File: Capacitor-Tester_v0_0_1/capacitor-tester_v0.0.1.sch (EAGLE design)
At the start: 34 parts, among them IC1 AD8531ARZ, IC2 MC34063EBD-TR, IC3 DAC6571IDBVT, IC5 AD8397ARDZ, J1 USB4125-GF-A-0190_REVA2, J2 DS1044-140G, J4 250-103, U1 AD5933, Y1 LFSPXO018034

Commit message: v0.0.1 - CMD renumber + tnames + bnames
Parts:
- removed IC5: AD8397ARDZ, AD8397ARDZ:AD8397ARDZ
- removed J4: 250-103, custom_library:250-103
- removed R15, R16: 10k-1%, custom_library:RESISTOR_SMD0603
- added IC4: MC34063EBD-TR, MC34063EBD-TR:MC34063EBD-TR
- added J3: USB4125-GF-A-0190_REVA2, USB-C-6Pin:USB4125-GF-A-0190_REVA2
- added R7, R8: DNP-4k7-1%, custom_library:RESISTOR_SMD0603
- C2: value 10u -> 100n
- C3: value 100n -> 10u
- C4: value 270u / 16V -> 10u; device EEEFKC271XSP:EEEFKC271XSP -> custom_library:CAPACITOR_SMD_CERAMIC0603
- C5: value 270u / 16V -> 100n; device EEEFKC271XSP:EEEFKC271XSP -> custom_library:CAPACITOR_SMD_CERAMIC0603
- C6: value 560p -> 270u / 16V; device custom_library:CAPACITOR_SMD_CERAMIC0603 -> EEEFKC271XSP:EEEFKC271XSP
- C7: value 100n -> 560p
- C8: value 10u -> 270u / 16V; device custom_library:CAPACITOR_SMD_CERAMIC0603 -> EEEFKC271XSP:EEEFKC271XSP
- D1: value SS14 -> PMEG6020ER,115; device SS14:SS14 -> PMEG6020ER_115:PMEG6020ER,115
- D2: value PMEG6020ER,115 -> SS14; device PMEG6020ER_115:PMEG6020ER,115 -> SS14:SS14
- IC1: value AD8531ARZ -> DAC6571IDBVT; device AD8531ARZ:AD8531ARZ -> DAC6571IDBVT:DAC6571IDBVT
- IC2: value MC34063EBD-TR -> AD8397ARDZ; device MC34063EBD-TR:MC34063EBD-TR -> AD8397ARDZ:AD8397ARDZ
- IC3: value DAC6571IDBVT -> AD8531ARZ; device DAC6571IDBVT:DAC6571IDBVT -> AD8531ARZ:AD8531ARZ
- J1: value USB4125-GF-A-0190_REVA2 -> DS1044-140G; device USB-C-6Pin:USB4125-GF-A-0190_REVA2 -> DS1044-140G:DS1044-140G
- J2: value DS1044-140G -> 250-103; device DS1044-140G:DS1044-140G -> custom_library:250-103
- R1, R3: value DNP-4k7-1% -> 10k-1%
- R10: value 1k-1% -> R133-1%
- R11: value R133-1% -> 8k66-1%
- R12: value 180R-1% -> 1k-1%
- R2: value 10k-1% -> DNP-10k-1%
- R4: value DNP-10k-1% -> 1k-1%
- R6: value 1k-1% -> 10k-1%
- R9: value 8k66-1% -> 180R-1%
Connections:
- net +12V: now also C1.1, C6.+, D2.K, IC2.+VS, R11.1; no longer C3.1, C4.+, D1.K, IC5.+VS, R9.1
- net +5V: now also C3.1, C4.1, C5.1, C8.+, D1.K, IC1.VDD, IC3.V+, IC4.VCC, J3.VBUS, R10.1, R7.2, R8.2; no longer C1.1, C5.+, C7.1, C8.1, D2.K, IC1.V+, IC2.VCC, IC3.VDD, J1.VBUS, R1.2, R11.1, R3.2
- net DAC_OUT: now also IC1.VOUT, IC2.+IN2; no longer IC3.VOUT, IC5.+IN2
- net FUNC_GEN: now also J2.3, SJ1.1; no longer J4.3, SJ2.1
- net GND: now also C4.2, C5.2, C6.-, C8.-, IC1.A0, IC1.GND, IC2.-VS, IC2.EP, IC3.+IN_A, IC3.V-, IC4.GND, IC4.SWE, J3.GND, J3.SHIELD, R1.2, R12.2; no longer C4.-, C5.-, C6.2, C8.2, IC1.+IN_A, IC1.V-, IC2.GND, IC2.SWE, IC3.A0, IC3.GND, IC5.-VS, IC5.EP, J1.GND, J1.SHIELD, R10.2, R15.2
- net MCLK: now also SJ2.1; no longer SJ1.1
- net N$1: now also IC3.OUT_A, R2.2, R3.1; no longer IC1.OUT_A, R2.1, R4.2
- net N$10: now also C7.1, IC4.TC; no longer C6.1, IC2.TC
- net N$11: now also IC4.IPK, R10.2, R9.2; no longer IC2.IPK, R11.2, R12.2
- net N$13: now also IC2.-IN2, R1.1, R6.2; no longer IC5.-IN2, R15.1, R16.2
- net N$4: now also IC2.-IN1, R4.1; no longer IC5.-IN1, R6.1
- net N$5: now also D2.A, IC4.SWC; no longer D1.A, IC2.SWC
- net N$7: now also IC4.CII, R11.2, R12.1; no longer IC2.CII, R10.1, R9.2
- net N$8: now also IC4.DRC, R9.1; no longer IC2.DRC, R12.1
- net SCL: now also IC1.SCL, J2.2, R8.1; no longer IC3.SCL, J4.2, R1.1
- net SDA: now also IC1.SDA, J2.1, R7.1; no longer IC3.SDA, J4.1, R3.1
- net UZA_OUT: now also IC2.OUT1, J1.1, J1.2, J1.3, J1.4, J1.5, J1.6, J1.7, R4.2; no longer IC5.OUT1, J2.1, J2.2, J2.3, J2.4, J2.5, J2.6, J2.7, R6.2
- net UZB_OUT: now also IC2.+IN1, IC2.OUT2, R6.1; no longer IC5.+IN1, IC5.OUT2, R16.1
- net VIN: now also R2.1; no longer R4.1
- net Z_OUT: now also D1.A, IC3.-IN_A, J1.10, J1.11, J1.12, J1.13, J1.14, J1.8, J1.9, R3.2; no longer D2.A, IC1.-IN_A, J2.10, J2.11, J2.12, J2.13, J2.14, J2.8, J2.9, R2.2
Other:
- moved on the sheet: C1, C2, C3, C7, D1, D2, R1, R10, R11, R12, R2, R3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

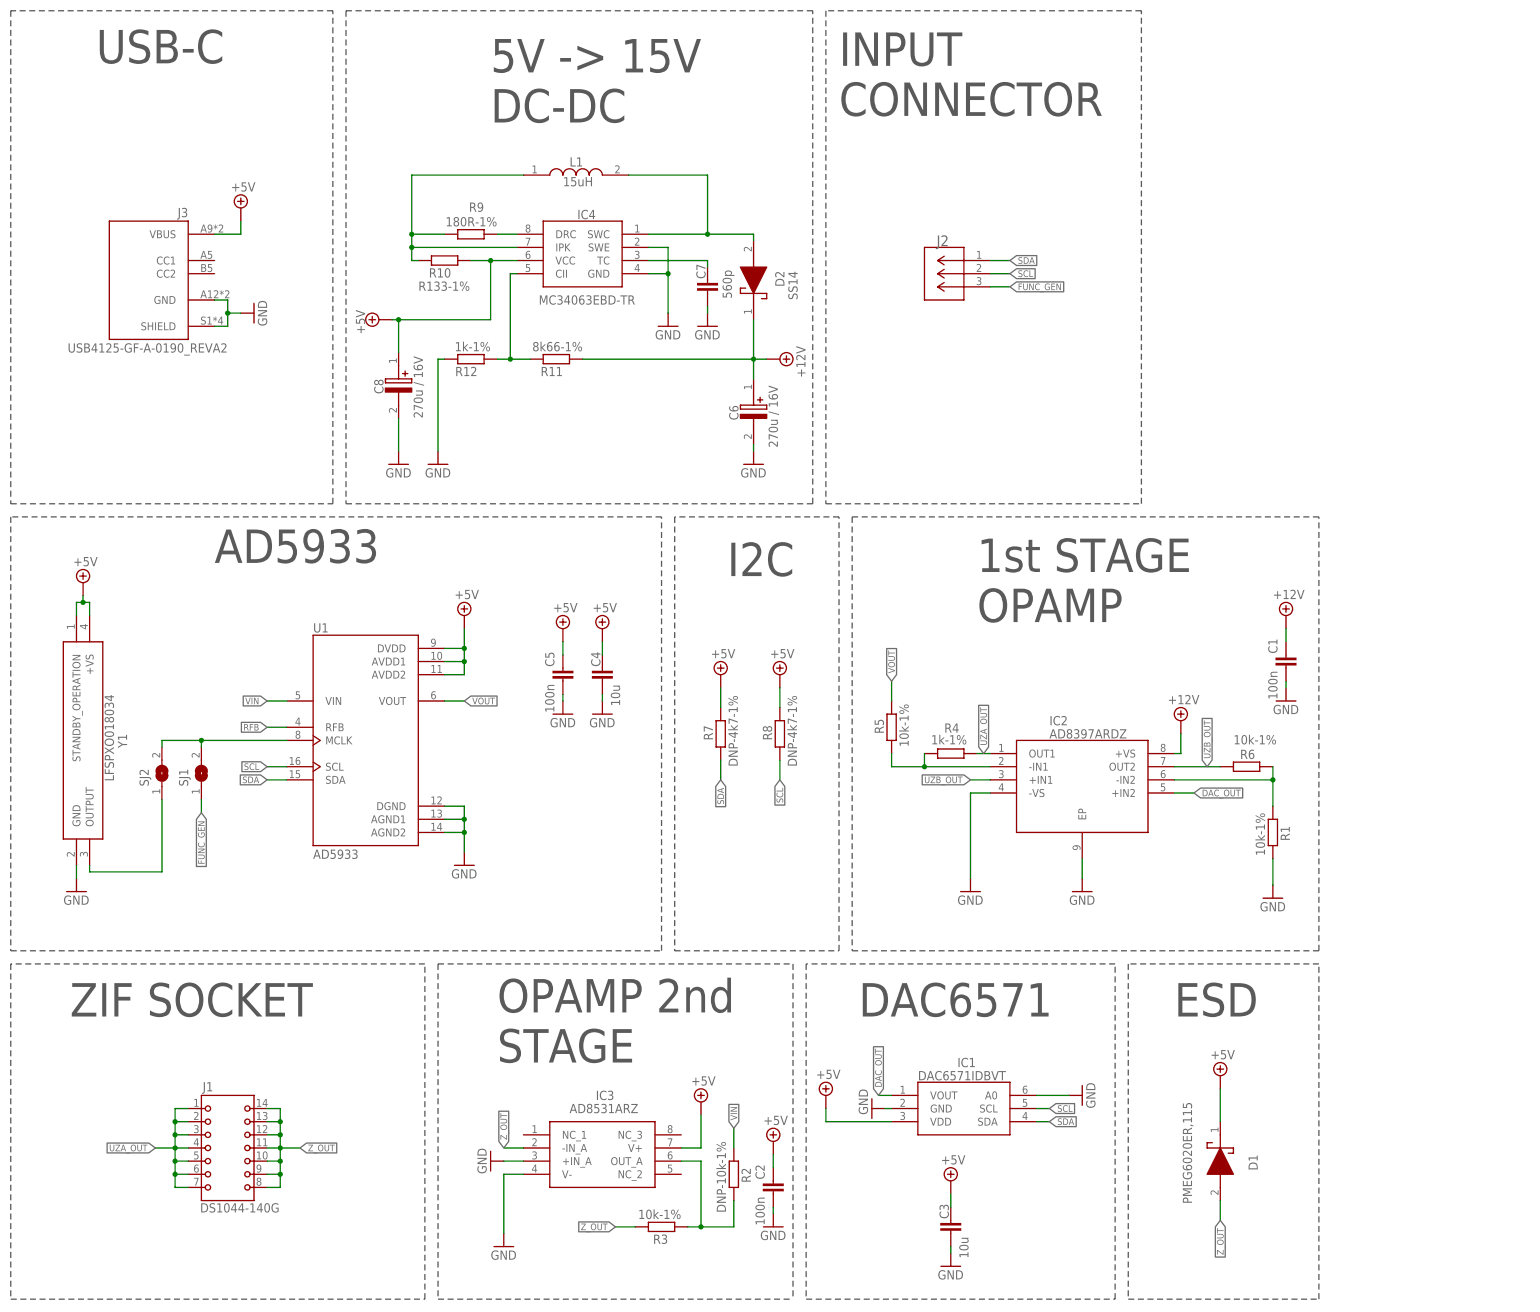
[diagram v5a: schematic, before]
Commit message: v0.0.1 - Different component layout and trace placement
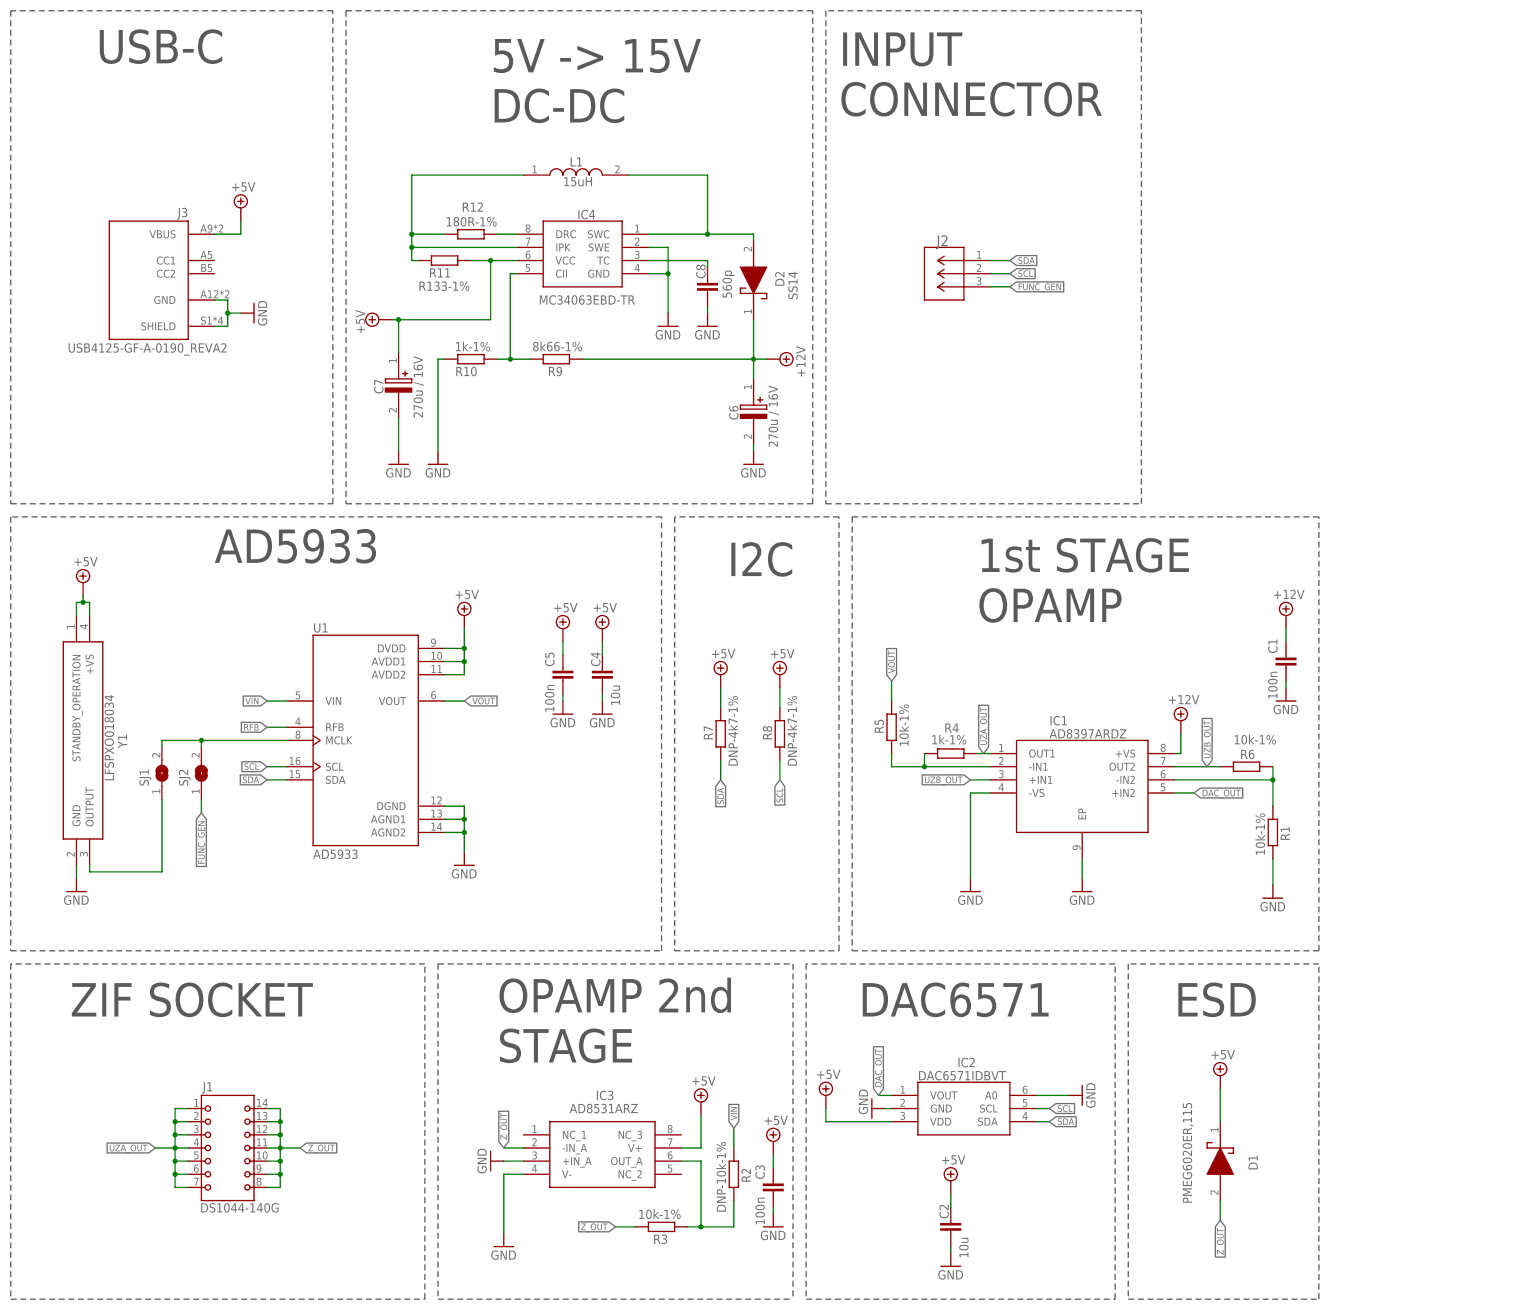
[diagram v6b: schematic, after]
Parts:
- C2: value 100n -> 10u
- C3: value 10u -> 100n
- C7: value 560p -> 270u / 16V; device custom_library:CAPACITOR_SMD_CERAMIC0603 -> EEEFKC271XSP:EEEFKC271XSP
- C8: value 270u / 16V -> 560p; device EEEFKC271XSP:EEEFKC271XSP -> custom_library:CAPACITOR_SMD_CERAMIC0603
- IC1: value DAC6571IDBVT -> AD8397ARDZ; device DAC6571IDBVT:DAC6571IDBVT -> AD8397ARDZ:AD8397ARDZ
- IC2: value AD8397ARDZ -> DAC6571IDBVT; device AD8397ARDZ:AD8397ARDZ -> DAC6571IDBVT:DAC6571IDBVT
- R10: value R133-1% -> 1k-1%
- R11: value 8k66-1% -> R133-1%
- R12: value 1k-1% -> 180R-1%
- R9: value 180R-1% -> 8k66-1%
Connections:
- net +12V: now also IC1.+VS, R9.1; no longer IC2.+VS, R11.1
- net +5V: now also C7.+, IC2.VDD, R11.1; no longer C8.+, IC1.VDD, R10.1
- net DAC_OUT: now also IC1.+IN2, IC2.VOUT; no longer IC1.VOUT, IC2.+IN2
- net FUNC_GEN: now also SJ2.1; no longer SJ1.1
- net GND: now also C7.-, C8.2, IC1.-VS, IC1.EP, IC2.A0, IC2.GND, R10.2; no longer C7.2, C8.-, IC1.A0, IC1.GND, IC2.-VS, IC2.EP, R12.2
- net MCLK: now also SJ1.1; no longer SJ2.1
- net N$10: now also C8.1; no longer C7.1
- net N$11: now also R11.2, R12.2; no longer R10.2, R9.2
- net N$13: now also IC1.-IN2; no longer IC2.-IN2
- net N$4: now also IC1.-IN1; no longer IC2.-IN1
- net N$7: now also R10.1, R9.2; no longer R11.2, R12.1
- net N$8: now also R12.1; no longer R9.1
- net SCL: now also IC2.SCL; no longer IC1.SCL
- net SDA: now also IC2.SDA; no longer IC1.SDA
- net UZA_OUT: now also IC1.OUT1; no longer IC2.OUT1
- net UZB_OUT: now also IC1.+IN1, IC1.OUT2; no longer IC2.+IN1, IC2.OUT2
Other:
- moved on the sheet: C2, C3, R10, R11, R12, R9, SJ1, SJ2

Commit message: V0.0.1 - Finished .brd
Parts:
- C1: value 100n -> 270u / 16V; device custom_library:CAPACITOR_SMD_CERAMIC0603 -> EEEFKC271XSP:EEEFKC271XSP
- C2: value 10u -> 560p
- C3: value 100n -> 10u
- C6, C7: value 270u / 16V -> 100n; device EEEFKC271XSP:EEEFKC271XSP -> custom_library:CAPACITOR_SMD_CERAMIC0603
- C8: value 560p -> 270u / 16V; device custom_library:CAPACITOR_SMD_CERAMIC0603 -> EEEFKC271XSP:EEEFKC271XSP
- D1: value PMEG6020ER,115 -> SS14; device PMEG6020ER_115:PMEG6020ER,115 -> SS14:SS14
- D2: value SS14 -> PMEG6020ER,115; device SS14:SS14 -> PMEG6020ER_115:PMEG6020ER,115
- IC1: value AD8397ARDZ -> MC34063EBD-TR; device AD8397ARDZ:AD8397ARDZ -> MC34063EBD-TR:MC34063EBD-TR
- IC3: value AD8531ARZ -> AD8397ARDZ; device AD8531ARZ:AD8531ARZ -> AD8397ARDZ:AD8397ARDZ
- IC4: value MC34063EBD-TR -> AD8531ARZ; device MC34063EBD-TR:MC34063EBD-TR -> AD8531ARZ:AD8531ARZ
- R1: value 10k-1% -> 8k66-1%
- R10: value 1k-1% -> R133-1%
- R11: value R133-1% -> DNP-4k7-1%
- R12: value 180R-1% -> DNP-4k7-1%
- R2: value DNP-10k-1% -> 1k-1%
- R4: value 1k-1% -> 10k-1%
- R6: value 10k-1% -> DNP-10k-1%
- R7: value DNP-4k7-1% -> 180R-1%
- R8: value DNP-4k7-1% -> 1k-1%
- R9: value 8k66-1% -> 10k-1%
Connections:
- net +12V: now also C1.+, C7.1, D1.K, IC3.+VS, R1.1; no longer C1.1, C6.+, D2.K, IC1.+VS, R9.1
- net +5V: now also C6.1, C8.+, D2.K, IC1.VCC, IC4.V+, R10.1, R11.2, R12.2; no longer C2.1, C7.+, D1.K, IC3.V+, IC4.VCC, R11.1, R7.2, R8.2
- net DAC_OUT: now also IC3.+IN2; no longer IC1.+IN2
- net GND: now also C1.-, C6.2, C7.2, C8.-, IC1.GND, IC1.SWE, IC3.-VS, IC3.EP, IC4.+IN_A, IC4.V-, R2.2, R4.2; no longer C1.2, C6.-, C7.-, C8.2, IC1.-VS, IC1.EP, IC3.+IN_A, IC3.V-, IC4.GND, IC4.SWE, R1.2, R10.2
- net N$1: now also IC4.OUT_A, R6.2, R9.1; no longer IC3.OUT_A, R2.2, R3.1
- net N$10: now also C2.1, IC1.TC; no longer C8.1, IC4.TC
- net N$11: now also IC1.IPK, R10.2, R7.2; no longer IC4.IPK, R11.2, R12.2
- net N$13: now also IC3.-IN2, R3.2, R4.1; no longer IC1.-IN2, R1.1, R6.2
- net N$4: now also IC3.-IN1, R8.1; no longer IC1.-IN1, R4.1
- net N$5: now also D1.A, IC1.SWC; no longer D2.A, IC4.SWC
- net N$7: now also IC1.CII, R1.2, R2.1; no longer IC4.CII, R10.1, R9.2
- net N$8: now also IC1.DRC, R7.1; no longer IC4.DRC, R12.1
- net SCL: now also R11.1; no longer R8.1
- net SDA: now also R12.1; no longer R7.1
- net UZA_OUT: now also IC3.OUT1, R8.2; no longer IC1.OUT1, R4.2
- net UZB_OUT: now also IC3.+IN1, IC3.OUT2, R3.1; no longer IC1.+IN1, IC1.OUT2, R6.1
- net VIN: now also R6.1; no longer R2.1
- net Z_OUT: now also D2.A, IC4.-IN_A, R9.2; no longer D1.A, IC3.-IN_A, R3.2
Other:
- moved on the sheet: C2, C3, D1, D2, IC4, R1, R10, R11, R12, R2, R3, R4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
